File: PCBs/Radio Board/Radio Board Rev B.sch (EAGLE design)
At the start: 4 parts

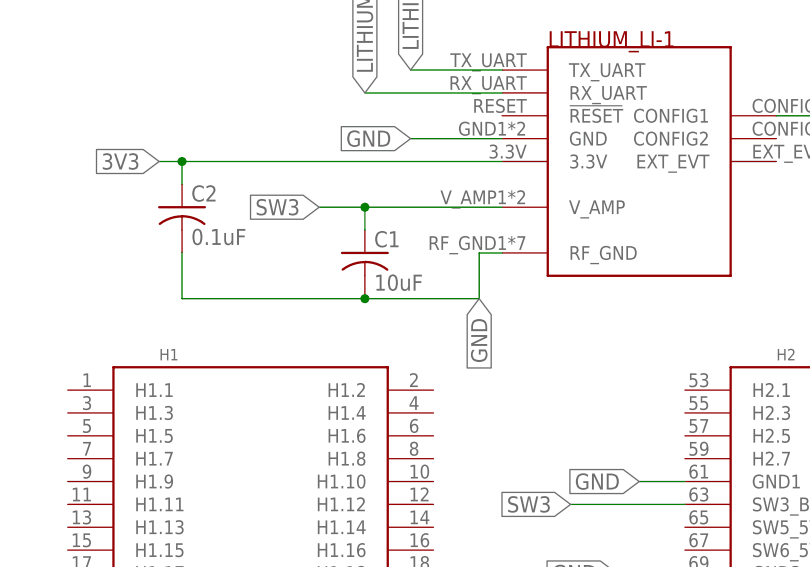
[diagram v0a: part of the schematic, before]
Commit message: Update cap values
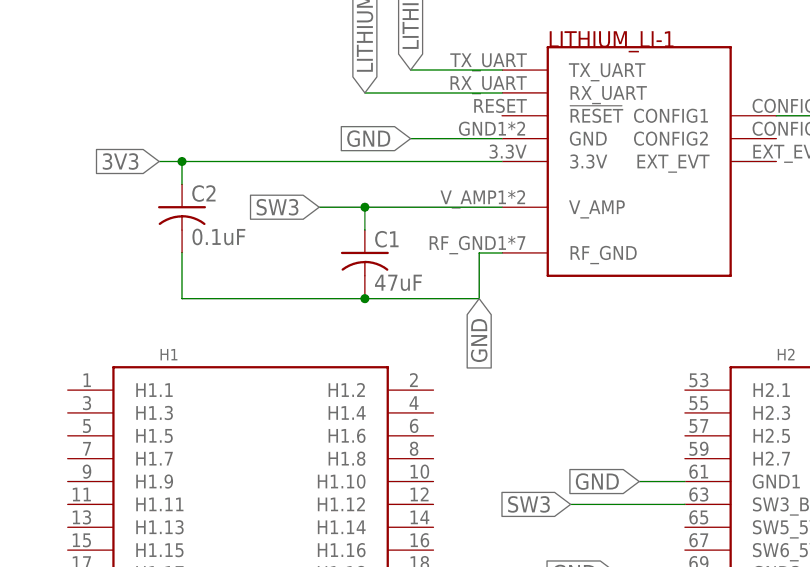
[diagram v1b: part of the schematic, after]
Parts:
- C1: value 10uF -> 47uF
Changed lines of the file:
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@@
 </classes>
 <parts>
-<part name="C1" library="resistor" library_urn="urn:adsk.eagle:library:348" deviceset="C-US" device="C0805" package3d_urn="urn:adsk.eagle:package:26137/1" value="10uF"/>
+<part name="C1" library="resistor" library_urn="urn:adsk.eagle:library:348" deviceset="C-US" device="C0805" package3d_urn="urn:adsk.eagle:package:26137/1" value="47uF"/>
 <part name="C2" library="resistor" library_urn="urn:adsk.eagle:library:348" deviceset="C-US" device="C0805" package3d_urn="urn:adsk.eagle:package:26137/1" value="0.1uF"/>
 <part name="LI-1" library="Cubesat" deviceset="LI-1" device=""/>

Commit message: Use common PC104 footprint with dimensions set per board
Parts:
- removed U$2: PC104_RADIO, Cubesat:PC104_RADIO
- added U$1: PC104_NO_DIMENSION, Cubesat:PC104_NO_DIMENSION
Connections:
- net 3V3: now also U$1.3V3BUS1; no longer U$2.3V3BUS1
- net GND: now also U$1.GND1, U$1.GND10, U$1.GND2, U$1.GND3, U$1.GND4, U$1.GND5, U$1.GND6, U$1.GND7, U$1.GND8, U$1.GND9; no longer U$2.GND1, U$2.GND10, U$2.GND2, U$2.GND3, U$2.GND4, U$2.GND5, U$2.GND6, U$2.GND7, U$2.GND8, U$2.GND9
- net LITHIUM_RX: now also U$1.LI_RX; no longer U$2.LI_RX
- net LITHIUM_TX: now also U$1.LI_TX; no longer U$2.LI_TX
- net OA_RESET: now also U$1.LI_OA_RST; no longer U$2.LI_OA_RST
- net SW3: now also U$1.SW3_BAT; no longer U$2.SW3_BAT
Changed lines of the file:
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@@
 <part name="C2" library="resistor" library_urn="urn:adsk.eagle:library:348" deviceset="C-US" device="C0805" package3d_urn="urn:adsk.eagle:package:26137/1" value="0.1uF"/>
 <part name="LI-1" library="Cubesat" deviceset="LI-1" device=""/>
-<part name="U$2" library="Cubesat" deviceset="PC104_RADIO" device=""/>
+<part name="U$1" library="Cubesat" deviceset="PC104_NO_DIMENSION" device=""/>
 </parts>
 <sheets>
@@
 <instance part="C2" gate="G$1" x="35.56" y="86.36"/>
 <instance part="LI-1" gate="G$1" x="76.2" y="78.74"/>
-<instance part="U$2" gate="A" x="22.86" y="66.04"/>
+<instance part="U$1" gate="A" x="22.86" y="66.04"/>
 </instances>
 <busses>
@@
 <wire x1="91.44" y1="55.88" x2="86.36" y2="55.88" width="0.1524" layer="91"/>
 <label x="86.36" y="55.88" size="1.778" layer="95" rot="R180" xref="yes"/>
-<pinref part="U$2" gate="A" pin="GND1"/>
+<pinref part="U$1" gate="A" pin="GND1"/>
 </segment>
 <segment>
 <wire x1="132.08" y1="40.64" x2="147.32" y2="40.64" width="0.1524" layer="91"/>
 <label x="147.32" y="40.64" size="1.778" layer="95" xref="yes"/>
-<pinref part="U$2" gate="A" pin="GND5"/>
+<pinref part="U$1" gate="A" pin="GND5"/>
 </segment>
 <segment>
@@
 <wire x1="91.44" y1="40.64" x2="83.82" y2="40.64" width="0.1524" layer="91"/>
 <label x="83.82" y="40.64" size="1.778" layer="95" rot="R180" xref="yes"/>
-<pinref part="U$2" gate="A" pin="GND4"/>
+<pinref part="U$1" gate="A" pin="GND4"/>
 </segment>
 <segment>
 <wire x1="132.08" y1="50.8" x2="137.16" y2="50.8" width="0.1524" layer="91"/>
 <label x="137.16" y="50.8" size="1.778" layer="95" xref="yes"/>
-<pinref part="U$2" gate="A" pin="GND2"/>
+<pinref part="U$1" gate="A" pin="GND2"/>
 </segment>
 <segment>
 <wire x1="91.44" y1="45.72" x2="83.82" y2="45.72" width="0.1524" layer="91"/>
 <label x="83.82" y="45.72" size="1.778" layer="95" rot="R180" xref="yes"/>
-<pinref part="U$2" gate="A" pin="GND3"/>
+<pinref part="U$1" gate="A" pin="GND3"/>
 </segment>
 <segment>
 <wire x1="91.44" y1="30.48" x2="83.82" y2="30.48" width="0.1524" layer="91"/>
 <label x="83.82" y="30.48" size="1.778" layer="95" rot="R180" xref="yes"/>
-<pinref part="U$2" gate="A" pin="GND6"/>
+<pinref part="U$1" gate="A" pin="GND6"/>
 </segment>
 <segment>
 <wire x1="91.44" y1="7.62" x2="83.82" y2="7.62" width="0.1524" layer="91"/>
 <label x="83.82" y="7.62" size="1.778" layer="95" rot="R180" xref="yes"/>
-<pinref part="U$2" gate="A" pin="GND9"/>
+<pinref part="U$1" gate="A" pin="GND9"/>
 </segment>
 <segment>
 <wire x1="132.08" y1="30.48" x2="137.16" y2="30.48" width="0.1524" layer="91"/>
 <label x="137.16" y="30.48" size="1.778" layer="95" xref="yes"/>
-<pinref part="U$2" gate="A" pin="GND7"/>
+<pinref part="U$1" gate="A" pin="GND7"/>
 </segment>
 <segment>
 <wire x1="132.08" y1="27.94" x2="144.78" y2="27.94" width="0.1524" layer="91"/>
 <label x="144.78" y="27.94" size="1.778" layer="95" xref="yes"/>
-<pinref part="U$2" gate="A" pin="GND8"/>
+<pinref part="U$1" gate="A" pin="GND8"/>
 </segment>
 <segment>
 <wire x1="132.08" y1="7.62" x2="137.16" y2="7.62" width="0.1524" layer="91"/>
 <label x="137.16" y="7.62" size="1.778" layer="95" xref="yes"/>
-<pinref part="U$2" gate="A" pin="GND10"/>
+<pinref part="U$1" gate="A" pin="GND10"/>
 </segment>
 <segment>
@@
 <wire x1="91.44" y1="53.34" x2="78.74" y2="53.34" width="0.1524" layer="91"/>
 <label x="78.74" y="53.34" size="1.778" layer="95" rot="R180" xref="yes"/>
-<pinref part="U$2" gate="A" pin="SW3_BAT"/>
+<pinref part="U$1" gate="A" pin="SW3_BAT"/>
 </segment>
 <segment>
@@
 <wire x1="22.86" y1="27.94" x2="10.16" y2="27.94" width="0.1524" layer="91"/>
 <label x="10.16" y="27.94" size="1.778" layer="95" rot="R180"/>
-<pinref part="U$2" gate="A" pin="LI_TX"/>
+<pinref part="U$1" gate="A" pin="LI_TX"/>
 </segment>
 </net>
@@
 <wire x1="22.86" y1="30.48" x2="10.16" y2="30.48" width="0.1524" layer="91"/>
 <label x="10.16" y="30.48" size="1.778" layer="95" rot="R180"/>
-<pinref part="U$2" gate="A" pin="LI_RX"/>
+<pinref part="U$1" gate="A" pin="LI_RX"/>
 </segment>
 </net>
@@
 <wire x1="91.44" y1="33.02" x2="76.2" y2="33.02" width="0.1524" layer="91"/>
 <label x="76.2" y="33.02" size="1.778" layer="95" rot="R180" xref="yes"/>
-<pinref part="U$2" gate="A" pin="3V3BUS1"/>
+<pinref part="U$1" gate="A" pin="3V3BUS1"/>
 </segment>
 <segment>
@@
 <wire x1="22.86" y1="7.62" x2="10.16" y2="7.62" width="0.1524" layer="91"/>
 <label x="10.16" y="7.62" size="1.778" layer="95" rot="R180"/>
-<pinref part="U$2" gate="A" pin="LI_OA_RST"/>
+<pinref part="U$1" gate="A" pin="LI_OA_RST"/>
 </segment>
 </net>

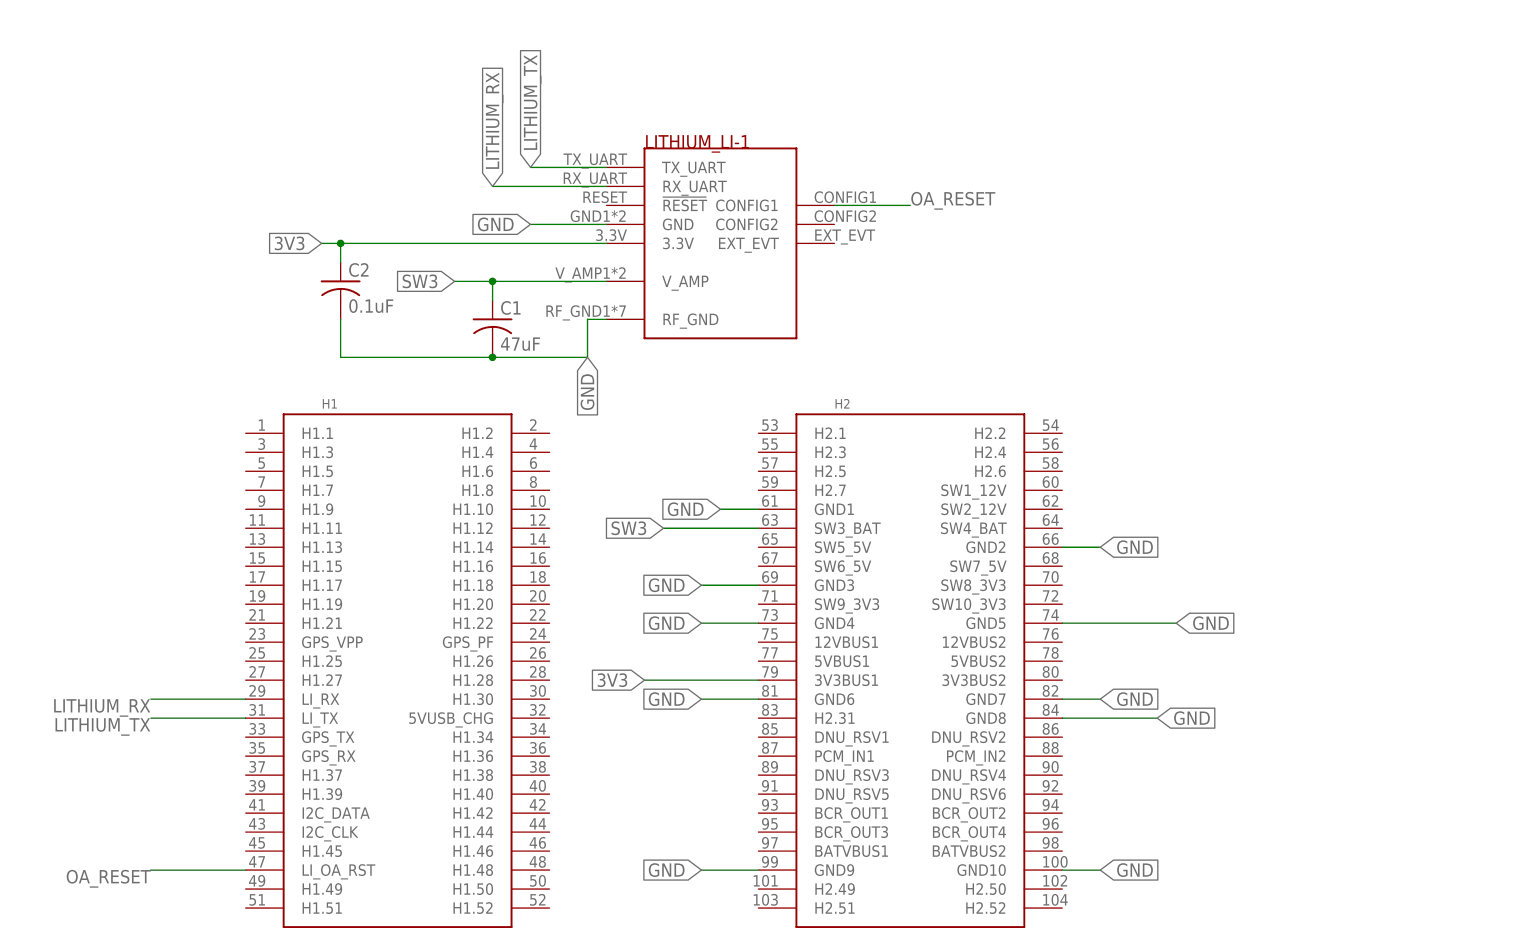
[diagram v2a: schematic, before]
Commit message: Add test pads
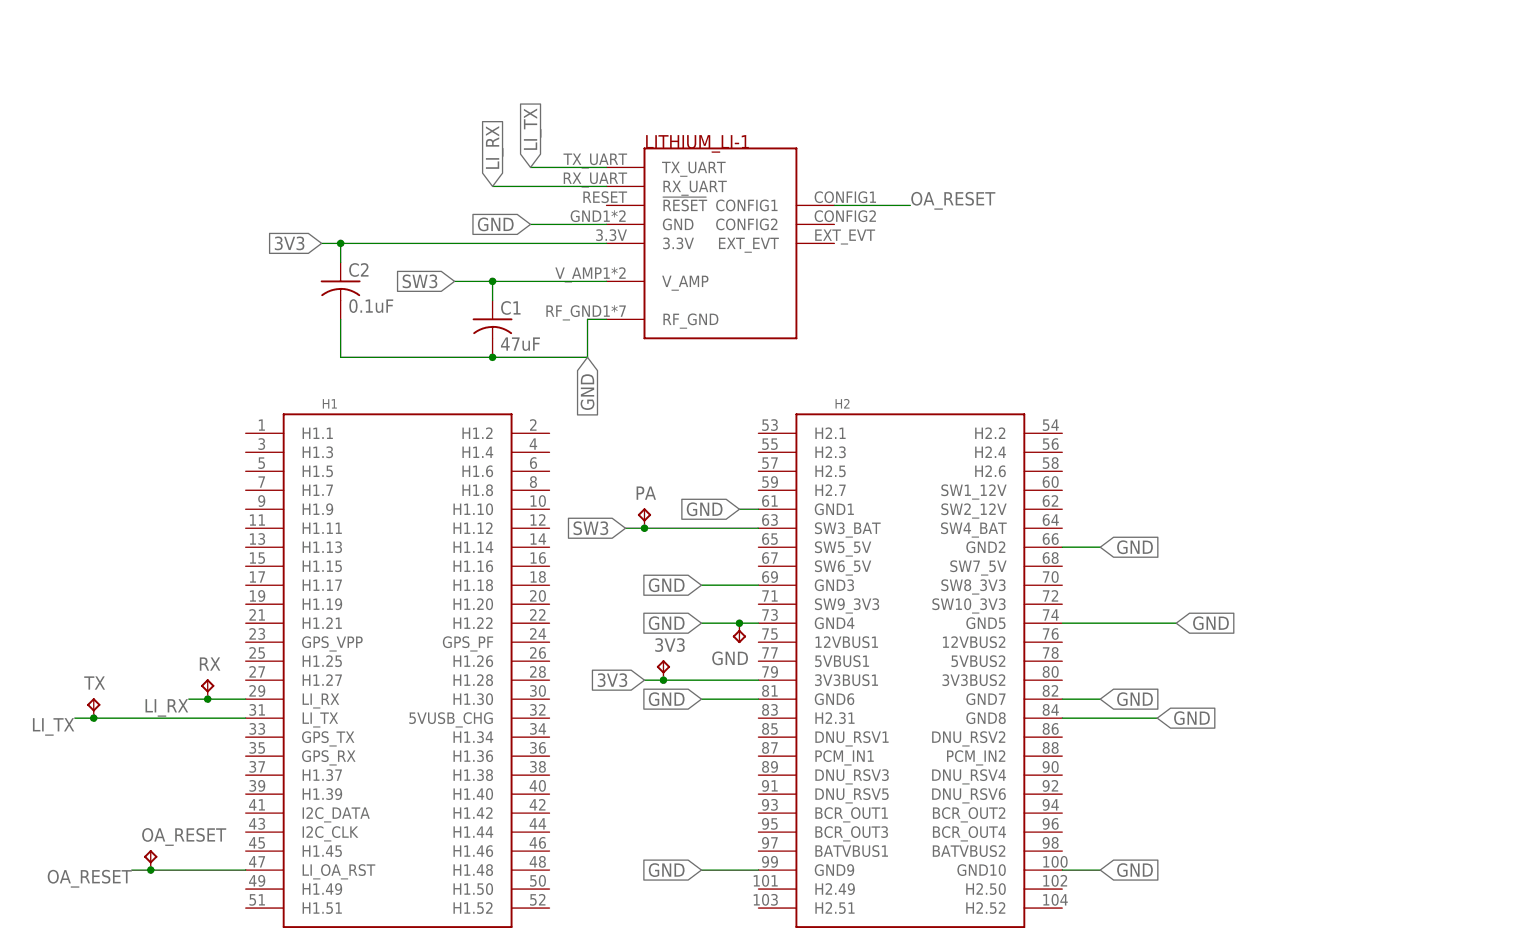
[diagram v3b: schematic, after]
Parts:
- added 3V3, GND, OA_RESET, PA, RX, TX: TPTP10SQ, testpad:TPTP10SQ
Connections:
- removed net LITHIUM_RX: LI-1.RX_UART, U$1.LI_RX
- removed net LITHIUM_TX: LI-1.TX_UART, U$1.LI_TX
- new net LI_RX: LI-1.RX_UART, RX.TP, U$1.LI_RX
- new net LI_TX: LI-1.TX_UART, TX.TP, U$1.LI_TX
- net 3V3: now also 3V3.TP
- net GND: now also GND.TP
- net OA_RESET: now also OA_RESET.TP
- net SW3: now also PA.TP
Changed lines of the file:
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@@
 <part name="LI-1" library="Cubesat" deviceset="LI-1" device=""/>
 <part name="U$1" library="Cubesat" deviceset="PC104_NO_DIMENSION" device=""/>
+<part name="3V3" library="testpad" library_urn="urn:adsk.eagle:library:385" deviceset="TP" device="TP10SQ" package3d_urn="urn:adsk.eagle:package:27962/1"/>
+<part name="RX" library="testpad" library_urn="urn:adsk.eagle:library:385" deviceset="TP" device="TP10SQ" package3d_urn="urn:adsk.eagle:package:27962/1"/>
+<part name="TX" library="testpad" library_urn="urn:adsk.eagle:library:385" deviceset="TP" device="TP10SQ" package3d_urn="urn:adsk.eagle:package:27962/1"/>
+<part name="OA_RESET" library="testpad" library_urn="urn:adsk.eagle:library:385" deviceset="TP" device="TP10SQ" package3d_urn="urn:adsk.eagle:package:27962/1"/>
+<part name="PA" library="testpad" library_urn="urn:adsk.eagle:library:385" deviceset="TP" device="TP10SQ" package3d_urn="urn:adsk.eagle:package:27962/1"/>
+<part name="GND" library="testpad" library_urn="urn:adsk.eagle:library:385" deviceset="TP" device="TP10SQ" package3d_urn="urn:adsk.eagle:package:27962/1"/>
 </parts>
 <sheets>
@@
 <instance part="LI-1" gate="G$1" x="76.2" y="78.74"/>
 <instance part="U$1" gate="A" x="22.86" y="66.04"/>
+<instance part="3V3" gate="G$1" x="78.74" y="35.56"/>
+<instance part="RX" gate="G$1" x="17.78" y="33.02"/>
+<instance part="TX" gate="G$1" x="2.54" y="30.48"/>
+<instance part="OA_RESET" gate="G$1" x="10.16" y="10.16"/>
+<instance part="PA" gate="G$1" x="76.2" y="55.88"/>
+<instance part="GND" gate="G$1" x="88.9" y="38.1" rot="R180"/>
 </instances>
 <busses>
@@
 <net name="GND" class="0">
 <segment>
-<wire x1="91.44" y1="55.88" x2="86.36" y2="55.88" width="0.1524" layer="91"/>
-<label x="86.36" y="55.88" size="1.778" layer="95" rot="R180" xref="yes"/>
+<wire x1="91.44" y1="55.88" x2="88.9" y2="55.88" width="0.1524" layer="91"/>
+<label x="88.9" y="55.88" size="1.778" layer="95" rot="R180" xref="yes"/>
 <pinref part="U$1" gate="A" pin="GND1"/>
 </segment>
@@
 </segment>
 <segment>
-<wire x1="91.44" y1="40.64" x2="83.82" y2="40.64" width="0.1524" layer="91"/>
+<wire x1="91.44" y1="40.64" x2="88.9" y2="40.64" width="0.1524" layer="91"/>
 <label x="83.82" y="40.64" size="1.778" layer="95" rot="R180" xref="yes"/>
 <pinref part="U$1" gate="A" pin="GND4"/>
+<pinref part="GND" gate="G$1" pin="TP"/>
+<wire x1="88.9" y1="40.64" x2="83.82" y2="40.64" width="0.1524" layer="91"/>
+<junction x="88.9" y="40.64"/>
 </segment>
 <segment>
@@
 <net name="SW3" class="0">
 <segment>
-<wire x1="91.44" y1="53.34" x2="78.74" y2="53.34" width="0.1524" layer="91"/>
-<label x="78.74" y="53.34" size="1.778" layer="95" rot="R180" xref="yes"/>
+<wire x1="91.44" y1="53.34" x2="76.2" y2="53.34" width="0.1524" layer="91"/>
+<label x="73.66" y="53.34" size="1.778" layer="95" rot="R180" xref="yes"/>
 <pinref part="U$1" gate="A" pin="SW3_BAT"/>
+<pinref part="PA" gate="G$1" pin="TP"/>
+<wire x1="76.2" y1="53.34" x2="73.66" y2="53.34" width="0.1524" layer="91"/>
+<junction x="76.2" y="53.34"/>
 </segment>
 <segment>
@@
 </segment>
 </net>
-<net name="LITHIUM_TX" class="0">
-<segment>
-<wire x1="71.12" y1="101.6" x2="60.96" y2="101.6" width="0.1524" layer="91"/>
-<label x="60.96" y="101.6" size="1.778" layer="95" rot="R90" xref="yes"/>
-<pinref part="LI-1" gate="G$1" pin="TX_UART"/>
-</segment>
-<segment>
-<wire x1="22.86" y1="27.94" x2="10.16" y2="27.94" width="0.1524" layer="91"/>
-<label x="10.16" y="27.94" size="1.778" layer="95" rot="R180"/>
-<pinref part="U$1" gate="A" pin="LI_TX"/>
-</segment>
-</net>
-<net name="LITHIUM_RX" class="0">
+<net name="LI_RX" class="0">
 <segment>
 <wire x1="71.12" y1="99.06" x2="55.88" y2="99.06" width="0.1524" layer="91"/>
@@
 </segment>
 <segment>
-<wire x1="22.86" y1="30.48" x2="10.16" y2="30.48" width="0.1524" layer="91"/>
-<label x="10.16" y="30.48" size="1.778" layer="95" rot="R180"/>
+<wire x1="22.86" y1="30.48" x2="17.78" y2="30.48" width="0.1524" layer="91"/>
+<label x="15.24" y="30.48" size="1.778" layer="95" rot="R180"/>
 <pinref part="U$1" gate="A" pin="LI_RX"/>
+<pinref part="RX" gate="G$1" pin="TP"/>
+<wire x1="17.78" y1="30.48" x2="15.24" y2="30.48" width="0.1524" layer="91"/>
+<junction x="17.78" y="30.48"/>
 </segment>
 </net>
 <net name="3V3" class="0">
 <segment>
-<wire x1="91.44" y1="33.02" x2="76.2" y2="33.02" width="0.1524" layer="91"/>
+<wire x1="91.44" y1="33.02" x2="78.74" y2="33.02" width="0.1524" layer="91"/>
 <label x="76.2" y="33.02" size="1.778" layer="95" rot="R180" xref="yes"/>
 <pinref part="U$1" gate="A" pin="3V3BUS1"/>
+<pinref part="3V3" gate="G$1" pin="TP"/>
+<wire x1="78.74" y1="33.02" x2="76.2" y2="33.02" width="0.1524" layer="91"/>
+<junction x="78.74" y="33.02"/>
 </segment>
 <segment>
@@
 <segment>
 <wire x1="22.86" y1="7.62" x2="10.16" y2="7.62" width="0.1524" layer="91"/>
-<label x="10.16" y="7.62" size="1.778" layer="95" rot="R180"/>
+<label x="7.62" y="7.62" size="1.778" layer="95" rot="R180"/>
 <pinref part="U$1" gate="A" pin="LI_OA_RST"/>
+<pinref part="OA_RESET" gate="G$1" pin="TP"/>
+<wire x1="10.16" y1="7.62" x2="7.62" y2="7.62" width="0.1524" layer="91"/>
+<junction x="10.16" y="7.62"/>
 </segment>
 </net>
+<net name="LI_TX" class="0">
+<segment>
+<wire x1="22.86" y1="27.94" x2="2.54" y2="27.94" width="0.1524" layer="91"/>
+<label x="0" y="27.94" size="1.778" layer="95" rot="R180"/>
+<pinref part="U$1" gate="A" pin="LI_TX"/>
+<pinref part="TX" gate="G$1" pin="TP"/>
+<wire x1="2.54" y1="27.94" x2="0" y2="27.94" width="0.1524" layer="91"/>
+<junction x="2.54" y="27.94"/>
+</segment>
+<segment>
+<wire x1="71.12" y1="101.6" x2="60.96" y2="101.6" width="0.1524" layer="91"/>
+<label x="60.96" y="101.6" size="1.778" layer="95" rot="R90" xref="yes"/>
+<pinref part="LI-1" gate="G$1" pin="TX_UART"/>
+</segment>
+</net>
